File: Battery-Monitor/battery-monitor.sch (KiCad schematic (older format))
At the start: 69 parts, among them J1 Conn_01x10_Male, J2 Conn_01x10_Male, J3 Conn_02x03_Odd_Even, U1 LMC6464, U2 LMC6464, U3 LMC6464, U4 LM285S-1.2, U5 ATtiny13-20SSU

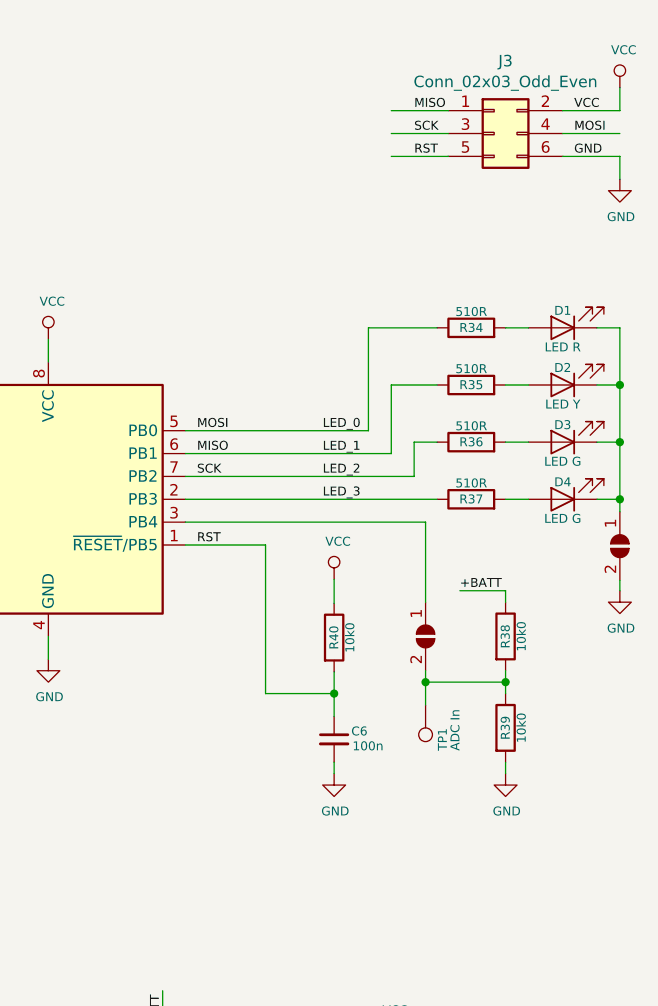
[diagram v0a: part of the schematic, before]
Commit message: Circuit tweaks
Added pull up/down resistor and solder bridge to allow mcu pick LED mode
at startup.  Added LPF to ADC input.
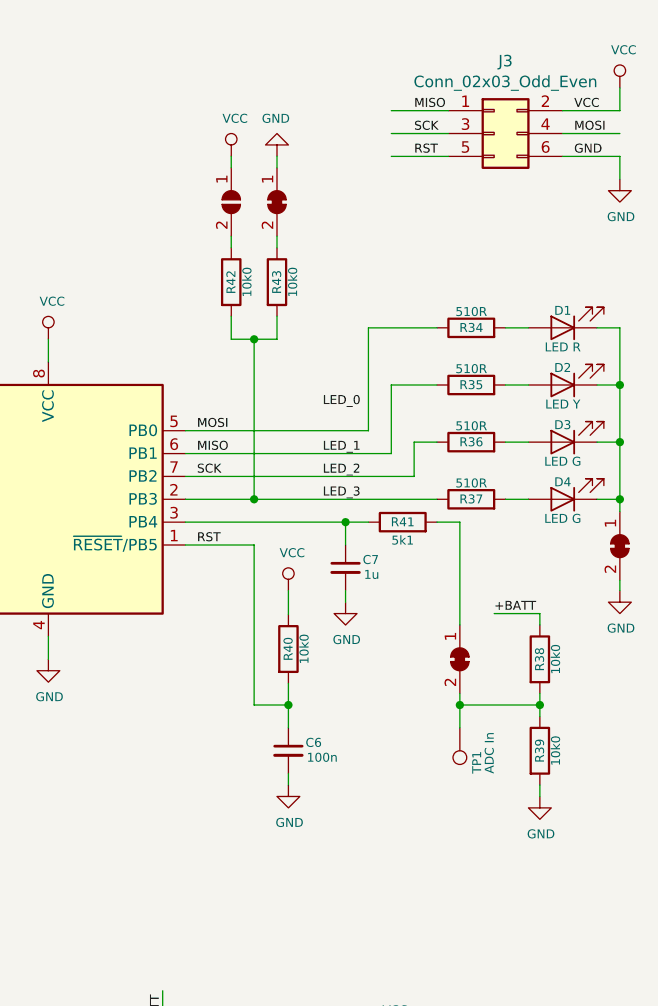
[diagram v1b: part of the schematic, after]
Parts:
- removed JP2: SolderJumper_2_Open, symbol Jumper:SolderJumper_2_Open
- added C7: 1u, symbol Device:C_Small
- added JP2, JP3, JP4: SolderJumper_2_Bridged, symbol Jumper:SolderJumper_2_Bridged
- added R41: 5k1, symbol Device:R
- added R42, R43: 10k0, symbol Device:R
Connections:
- wire segments 269 -> 283
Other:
- moved on the sheet: C6, R38, R39, R40, TP1

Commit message: begun pcb layout
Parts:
- removed J3: Conn_02x03_Odd_Even, symbol Connector_Generic:Conn_02x03_Odd_Even
- added J3: Conn_01x06_Male, Pin_Headers:Pin_Header_Straight_1x06_Pitch2.54mm, symbol Connector:Conn_01x06_Male
- added JP5: SolderJumper_2_Bridged, Jumper:SolderJumper-2_P1.3mm_Bridged_Pad1.0x1.5mm, symbol Jumper:SolderJumper_2_Bridged
- C1, C2, C3, C4, C5, C6, C7: footprint (none) -> Capacitors_SMD:C_0805_HandSoldering
- D1, D2, D3, D4: footprint (none) -> LEDs:LED_0805_HandSoldering
- J1, J2: footprint (none) -> Pin_Headers:Pin_Header_Straight_1x10_Pitch2.54mm
- JP1: footprint (none) -> Jumper:SolderJumper-2_P1.3mm_Open_Pad1.0x1.5mm
- JP2, JP3, JP4: footprint (none) -> Jumper:SolderJumper-2_P1.3mm_Bridged_Pad1.0x1.5mm
- R1, R10, R11, R12, R13, R14, R15, R16, R17, R18, R19, R2, R20, R21, R22, R23, R24, R25, R26, R27, R28, R29, R3, R30, R34, R35, R36, R37, R38, R39, R4, R40, R41, R42, R43, R5, R6, R7, R8, R9: footprint (none) -> Resistors_SMD:R_0603_HandSoldering
- R31, R32, R33: footprint (none) -> Resistors_SMD:R_0805_HandSoldering
- TP1, TP2, TP3, TP4, TP5, TP6, TP7, TP8, TP9: footprint (none) -> Measurement_Points:Measurement_Point_Round-SMD-Pad_Small
- U1, U2, U3: footprint (none) -> SMD_Packages:SOIC-14_N
- U4, U5: footprint Package_SO:SOIC-8_3.9x4.9mm_P1.27mm -> SMD_Packages:SOIC-8-N
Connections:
- net labels added: B_LED_0, B_LED_1, B_LED_2, B_LED_3, C_LED_1, C_LED_2, C_LED_3, C_LED_4, C_LED_5, C_LED_6
- net labels removed: LED_0, LED_1, LED_2, LED_3, LED_4, LED_5, LED_6
- wire segments 283 -> 284
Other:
- moved on the sheet: C6

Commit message: completed layoul
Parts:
- R34, R35, R36, R37, R38, R39, R40, R41, R42, R43: footprint Resistors_SMD:R_0603_HandSoldering -> Resistors_SMD:R_0805_HandSoldering
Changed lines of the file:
@@
 F 0 "R34" V 10350 1850 39  0000 C CNN
 F 1 "510R" V 10420 1850 39  0000 C CNN
-F 2 "Resistors_SMD:R_0603_HandSoldering" V 10280 1850 50  0001 C CNN
+F 2 "Resistors_SMD:R_0805_HandSoldering" V 10280 1850 50  0001 C CNN
 F 3 "~" H 10350 1850 50  0001 C CNN
 	1    10350 1850
@@
 F 0 "R35" V 10350 2100 39  0000 C CNN
 F 1 "510R" V 10420 2100 39  0000 C CNN
-F 2 "Resistors_SMD:R_0603_HandSoldering" V 10280 2100 50  0001 C CNN
+F 2 "Resistors_SMD:R_0805_HandSoldering" V 10280 2100 50  0001 C CNN
 F 3 "~" H 10350 2100 50  0001 C CNN
 	1    10350 2100
@@
 F 0 "R36" V 10350 2350 39  0000 C CNN
 F 1 "510R" V 10420 2350 39  0000 C CNN
-F 2 "Resistors_SMD:R_0603_HandSoldering" V 10280 2350 50  0001 C CNN
+F 2 "Resistors_SMD:R_0805_HandSoldering" V 10280 2350 50  0001 C CNN
 F 3 "~" H 10350 2350 50  0001 C CNN
 	1    10350 2350
@@
 F 0 "R37" V 10350 2600 39  0000 C CNN
 F 1 "510R" V 10420 2600 39  0000 C CNN
-F 2 "Resistors_SMD:R_0603_HandSoldering" V 10280 2600 50  0001 C CNN
+F 2 "Resistors_SMD:R_0805_HandSoldering" V 10280 2600 50  0001 C CNN
 F 3 "~" H 10350 2600 50  0001 C CNN
 	1    10350 2600
@@
 F 0 "R38" V 10650 3300 39  0000 C CNN
 F 1 "10k0" V 10720 3300 39  0000 C CNN
-F 2 "Resistors_SMD:R_0603_HandSoldering" V 10580 3300 50  0001 C CNN
+F 2 "Resistors_SMD:R_0805_HandSoldering" V 10580 3300 50  0001 C CNN
 F 3 "~" H 10650 3300 50  0001 C CNN
 	1    10650 3300
@@
 F 0 "R39" V 10650 3700 39  0000 C CNN
 F 1 "10k0" V 10720 3700 39  0000 C CNN
-F 2 "Resistors_SMD:R_0603_HandSoldering" V 10580 3700 50  0001 C CNN
+F 2 "Resistors_SMD:R_0805_HandSoldering" V 10580 3700 50  0001 C CNN
 F 3 "~" H 10650 3700 50  0001 C CNN
 	1    10650 3700
@@
 F 0 "R40" V 9550 3255 39  0000 C CNN
 F 1 "10k0" V 9620 3255 39  0000 C CNN
-F 2 "Resistors_SMD:R_0603_HandSoldering" V 9480 3255 50  0001 C CNN
+F 2 "Resistors_SMD:R_0805_HandSoldering" V 9480 3255 50  0001 C CNN
 F 3 "~" H 9550 3255 50  0001 C CNN
 	1    9550 3255
@@
 F 0 "R42" V 9300 1650 39  0000 C CNN
 F 1 "10k0" V 9370 1650 39  0000 C CNN
-F 2 "Resistors_SMD:R_0603_HandSoldering" V 9230 1650 50  0001 C CNN
+F 2 "Resistors_SMD:R_0805_HandSoldering" V 9230 1650 50  0001 C CNN
 F 3 "~" H 9300 1650 50  0001 C CNN
 	1    9300 1650
@@
 F 0 "R43" V 9500 1650 39  0000 C CNN
 F 1 "10k0" V 9570 1650 39  0000 C CNN
-F 2 "Resistors_SMD:R_0603_HandSoldering" V 9430 1650 50  0001 C CNN
+F 2 "Resistors_SMD:R_0805_HandSoldering" V 9430 1650 50  0001 C CNN
 F 3 "~" H 9500 1650 50  0001 C CNN
 	1    9500 1650
@@
 F 0 "R41" V 10050 2700 39  0000 C CNN
 F 1 "5k1" V 9970 2700 39  0000 C CNN
-F 2 "Resistors_SMD:R_0603_HandSoldering" V 9980 2700 50  0001 C CNN
+F 2 "Resistors_SMD:R_0805_HandSoldering" V 9980 2700 50  0001 C CNN
 F 3 "~" H 10050 2700 50  0001 C CNN
 	1    10050 2700
